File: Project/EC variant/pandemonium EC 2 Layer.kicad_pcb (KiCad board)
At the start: 2 copper layers, 190.5 x 81.6 mm, 105 parts, among them J1 USB_C_Receptacle_USB2.0, SW1 DFU, U11 PRTR5V0U2X, U5 OPA354, U6 74HC4051, U7 74HC4051, U8 STM32F072CBT6, U9 XC6206PxxxMR-Regulator_Linear

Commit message: small work on pandi EC and BLE
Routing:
- net ROW2: track 253.6 -> 261.1 mm
- net COL0: track 93.1 -> 96.6 mm
- net COL9: track 133.4 -> 131.5 mm
- net APLEX_OUT: track 128.0 -> 128.9 mm
- net GND: vias 188 -> 198

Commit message: BLE progress
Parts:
- moved G*** 0.79 mm to (174.6, 42.1)
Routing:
- net COL9: track 131.5 -> 115.9 mm
- net GND: vias 198 -> 196
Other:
- outline, holes or cut-outs redrawn

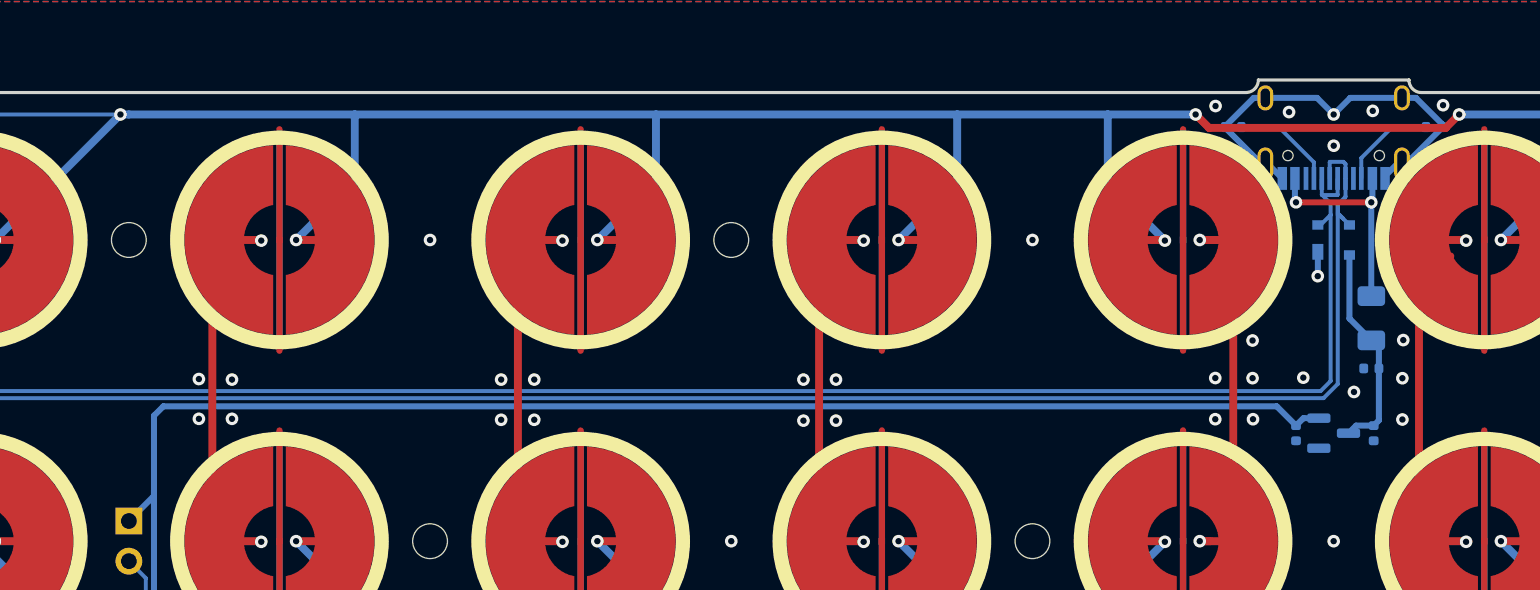
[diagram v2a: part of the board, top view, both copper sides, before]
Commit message: EC plates created
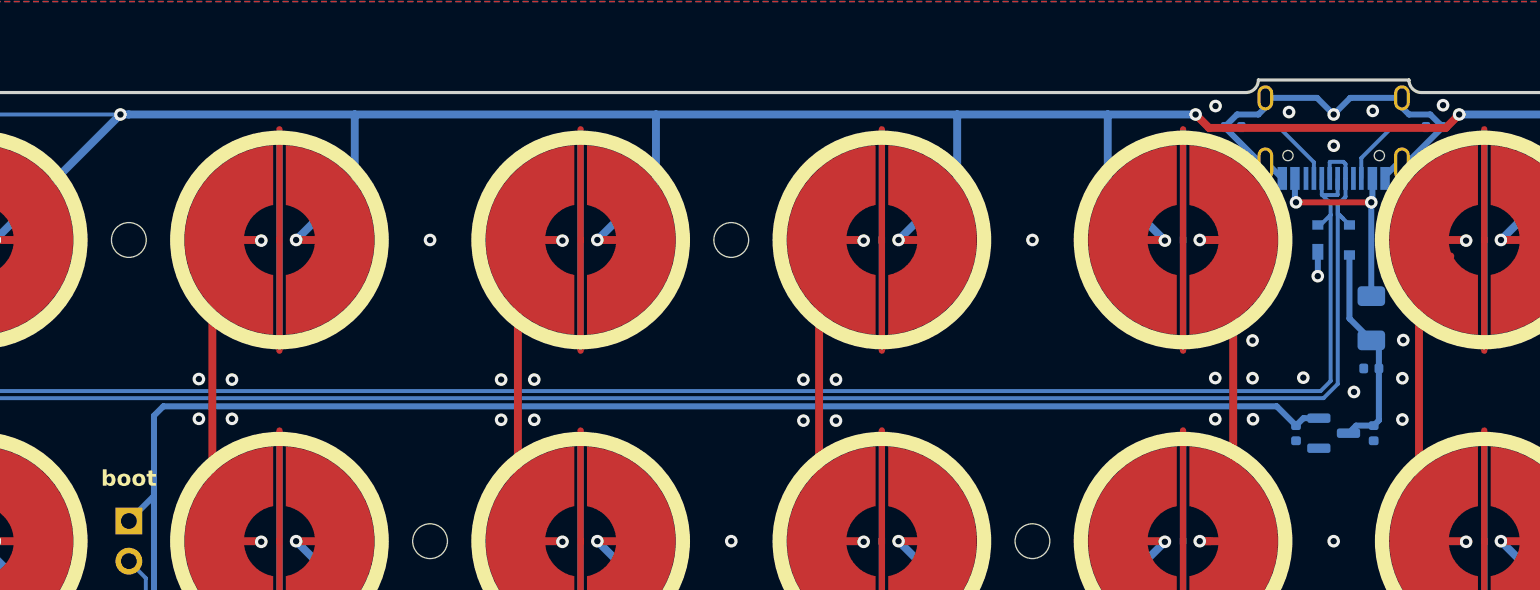
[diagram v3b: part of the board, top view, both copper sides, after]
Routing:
- net GND: track 74.9 -> 75.5 mm
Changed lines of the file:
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@@
     (effects (font (size 1 1) (thickness 0.15)) (justify bottom mirror))
-  )
-  (gr_text "boot" (at 50.8 48.41875) (layer "B.SilkS")
-    (effects (font (size 1 1) (thickness 0.2) bold) (justify mirror))
   )
   (gr_text "ISO" (at 219.86875 81.75625) (layer "B.SilkS")
@@
   (gr_text "concept by haizeus" (at 188.11875 101.6) (layer "F.SilkS")
     (effects (font (size 1 1) (thickness 0.2) bold) (justify left bottom))
+  )
+  (gr_text "boot" (at 50.8 48.41875) (layer "F.SilkS")
+    (effects (font (size 1 1) (thickness 0.2) bold))
   )
   (via (at 161.925 95.25) (size 0.8) (drill 0.4) (layers "F.Cu" "B.Cu") (net 0))
@@
   (via (at 119.512316 42.06875) (size 0.8) (drill 0.4) (layers "F.Cu" "B.Cu") (free) (net 8))
   (segment (start 131.566919 28.53) (end 131.32 28.53) (width 0.381) (layer "B.Cu") (net 8))
+  (segment (start 120.14 26.150581) (end 120.890581 25.4) (width 0.381) (layer "B.Cu") (net 8))
   (segment (start 60.764591 75.321651) (end 60.7545 75.31156) (width 0.25) (layer "B.Cu") (net 8))
   (segment (start 162.71875 80.535205) (end 162.722395 80.53156) (width 0.25) (layer "B.Cu") (net 8))
@@
   (segment (start 85.215 80.69375) (end 85.215 79.735164) (width 0.25) (layer "B.Cu") (net 8))
   (segment (start 56.35625 80.9625) (end 54.10625 83.2125) (width 0.25) (layer "B.Cu") (net 8))
-  (segment (start 132.201 24.35) (end 133.86 26.009) (width 0.381) (layer "B.Cu") (net 8))
   (segment (start 63.085811 81.215986) (end 63.974832 81.215986) (width 0.25) (layer "B.Cu") (net 8))
   (segment (start 167.693888 79.897984) (end 167.693888 80.305312) (width 0.25) (layer "B.Cu") (net 8))
@@
   (segment (start 58.915 74.406068) (end 58.917561 74.403507) (width 0.25) (layer "B.Cu") (net 8))
   (segment (start 58.60625 76.8) (end 58.60625 77.91875) (width 0.25) (layer "B.Cu") (net 8))
+  (segment (start 133.86 26.150581) (end 133.109419 25.4) (width 0.381) (layer "B.Cu") (net 8))
+  (segment (start 133.109419 25.4) (end 131.7625 25.4) (width 0.381) (layer "B.Cu") (net 8))
   (segment (start 120.14 26.236919) (end 122.433081 28.53) (width 0.381) (layer "B.Cu") (net 8))
   (segment (start 131.32 24.35) (end 128.05 24.35) (width 0.381) (layer "B.Cu") (net 8))
@@
   (segment (start 62.100319 75.321651) (end 60.764591 75.321651) (width 0.25) (layer "B.Cu") (net 8))
   (segment (start 128.05 24.35) (end 127 25.4) (width 0.381) (layer "B.Cu") (net 8))
+  (segment (start 133.86 26.19375) (end 133.86 26.150581) (width 0.381) (layer "B.Cu") (net 8))
   (segment (start 133.86 26.19375) (end 133.86 26.236919) (width 0.381) (layer "B.Cu") (net 8))
+  (segment (start 120.890581 25.4) (end 122.2375 25.4) (width 0.381) (layer "B.Cu") (net 8))
   (segment (start 58.915 75.269941) (end 58.915 74.406068) (width 0.25) (layer "B.Cu") (net 8))
   (segment (start 125.95 24.35) (end 122.68 24.35) (width 0.381) (layer "B.Cu") (net 8))
@@
   (segment (start 80.9625 81.27625) (end 80.9625 80.35351) (width 0.25) (layer "B.Cu") (net 8))
   (segment (start 61.9125 88.2625) (end 63.393254 88.2625) (width 0.25) (layer "B.Cu") (net 8))
-  (segment (start 120.14 26.150581) (end 120.14 26.19375) (width 0.381) (layer "B.Cu") (net 8))
+  (segment (start 131.32 24.9575) (end 131.32 24.35) (width 0.381) (layer "B.Cu") (net 8))
   (segment (start 173.0375 83.275249) (end 173.037499 83.275248) (width 0.25) (layer "B.Cu") (net 8))
   (segment (start 167.1975 80.8017) (end 167.48125 80.8017) (width 0.25) (layer "B.Cu") (net 8))
@@
   (segment (start 87.3125 89.41) (end 87.3125 90.347924) (width 0.25) (layer "B.Cu") (net 8))
   (segment (start 91.28125 86.235) (end 91.28125 87.3125) (width 0.25) (layer "B.Cu") (net 8))
-  (segment (start 131.32 24.35) (end 132.201 24.35) (width 0.381) (layer "B.Cu") (net 8))
+  (segment (start 131.7625 25.4) (end 131.32 24.9575) (width 0.381) (layer "B.Cu") (net 8))
   (segment (start 80.008984 83.34375) (end 80.006756 83.345978) (width 0.25) (layer "B.Cu") (net 8))
   (segment (start 162.71875 86.963923) (end 162.71875 87.756831) (width 0.25) (layer "B.Cu") (net 8))
@@
   (segment (start 131.01375 28.53) (end 130.175 29.36875) (width 0.381) (layer "B.Cu") (net 8))
   (segment (start 63.13 83.178076) (end 63.96826 83.178076) (width 0.25) (layer "B.Cu") (net 8))
+  (segment (start 120.14 26.19375) (end 120.14 26.150581) (width 0.381) (layer "B.Cu") (net 8))
   (segment (start 54.10625 83.2125) (end 54.10625 85.125) (width 0.25) (layer "B.Cu") (net 8))
   (segment (start 54.10625 78.7125) (end 52.19375 78.7125) (width 0.25) (layer "B.Cu") (net 8))
@@
   (segment (start 56.35625 80.16875) (end 56.35625 80.9625) (width 0.25) (layer "B.Cu") (net 8))
   (segment (start 62.070331 83.178076) (end 63.13 83.178076) (width 0.25) (layer "B.Cu") (net 8))
+  (segment (start 122.68 24.9575) (end 122.68 24.35) (width 0.381) (layer "B.Cu") (net 8))
   (segment (start 122.433081 28.53) (end 122.68 28.53) (width 0.381) (layer "B.Cu") (net 8))
-  (segment (start 122.68 24.35) (end 121.940581 24.35) (width 0.381) (layer "B.Cu") (net 8))
+  (segment (start 122.2375 25.4) (end 122.68 24.9575) (width 0.381) (layer "B.Cu") (net 8))
   (segment (start 58.2 87.79875) (end 58.2 88.2625) (width 0.25) (layer "B.Cu") (net 8))
   (segment (start 167.48125 80.8017) (end 168.15875 80.8017) (width 0.25) (layer "B.Cu") (net 8))
@@
   (segment (start 122.835 28.53) (end 123.75 29.445) (width 0.381) (layer "B.Cu") (net 8))
   (segment (start 120.14 26.19375) (end 120.14 26.236919) (width 0.381) (layer "B.Cu") (net 8))
-  (segment (start 121.940581 24.35) (end 120.14 26.150581) (width 0.381) (layer "B.Cu") (net 8))
   (segment (start 127 25.4) (end 125.95 24.35) (width 0.381) (layer "B.Cu") (net 8))
   (segment (start 51.990908 76.148536) (end 51.990908 75.15831) (width 0.25) (layer "B.Cu") (net 8))
   (segment (start 63.96826 83.178076) (end 63.980049 83.166287) (width 0.25) (layer "B.Cu") (net 8))
-  (segment (start 133.86 26.009) (end 133.86 26.19375) (width 0.381) (layer "B.Cu") (net 8))
   (segment (start 63.393254 88.2625) (end 63.401824 88.25393) (width 0.25) (layer "B.Cu") (net 8))
   (segment (start 51.994552 85.728644) (end 51.994552 86.682577) (width 0.25) (layer "B.Cu") (net 8))
@@
   (group "" (id 377a50c5-704e-4dd8-b33e-f719293d46e1)
     (members
+      04cd13ad-5de1-4dcd-84f3-68bd5c15e42d
       08f5fb85-67dd-4189-9deb-b619be47a99b
       0a63a150-cd52-4d2c-a11c-35eaa3b43195
@@
       2843f161-3406-4bbd-8334-7e606c2472a4
       34d02041-ab84-4668-bb44-895bbf7fed2d
+      3597e3fe-3ada-44cd-b700-c11a495881cb
+      36ce7fc6-0b1c-4818-8fd6-ddc8c779315d
       3859ece4-2a36-4010-a2cf-c9bdbe33ade4
       3f4b8926-b566-42fc-a39b-133517f73076
+      49a5c273-46b0-417a-a662-90483755195e
+      5bb5e31f-a416-425a-b1b5-24b7d94e6142
+      6391a184-2239-4162-a729-ff6d2c273af0
       6a715f4d-3b33-417c-bca4-d1377b91e0ca
       8e559473-98f4-40fe-a19d-a4422e6460e6
       9171ce5a-b6bc-420e-801e-8db979268b8c
+      a84a4f9d-f245-4b01-83e2-4a59b20f7506
+      b6e6f590-4d1c-414e-b88b-04aaaaaadec0
+      c3c60ae9-ccfd-46a9-b688-ae6b2f2ca8eb
+      ccfb383c-97d6-4b58-8060-b1a15dfda5c5
       d66ccce1-03c6-45ff-a2ee-1a5ddc59d1d2
     )
